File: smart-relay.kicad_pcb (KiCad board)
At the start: 2 copper layers, 16 parts, among them IC1 TMCS1101A4BQDR, J1 Screw_Terminal_01x03, J2 Conn_01x04, K1 G5LE-1, Q1 BSS138K, U1 OPAMP, U2 ATtiny85-20PU

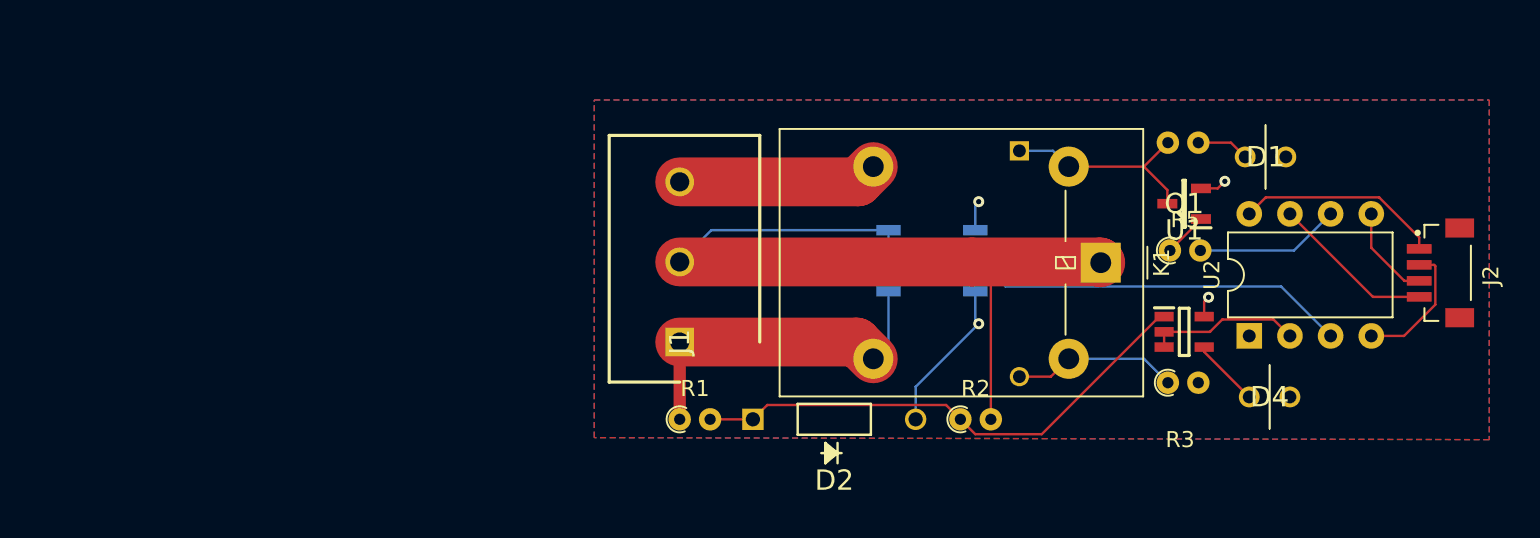
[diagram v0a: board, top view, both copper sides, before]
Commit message: separate hv line
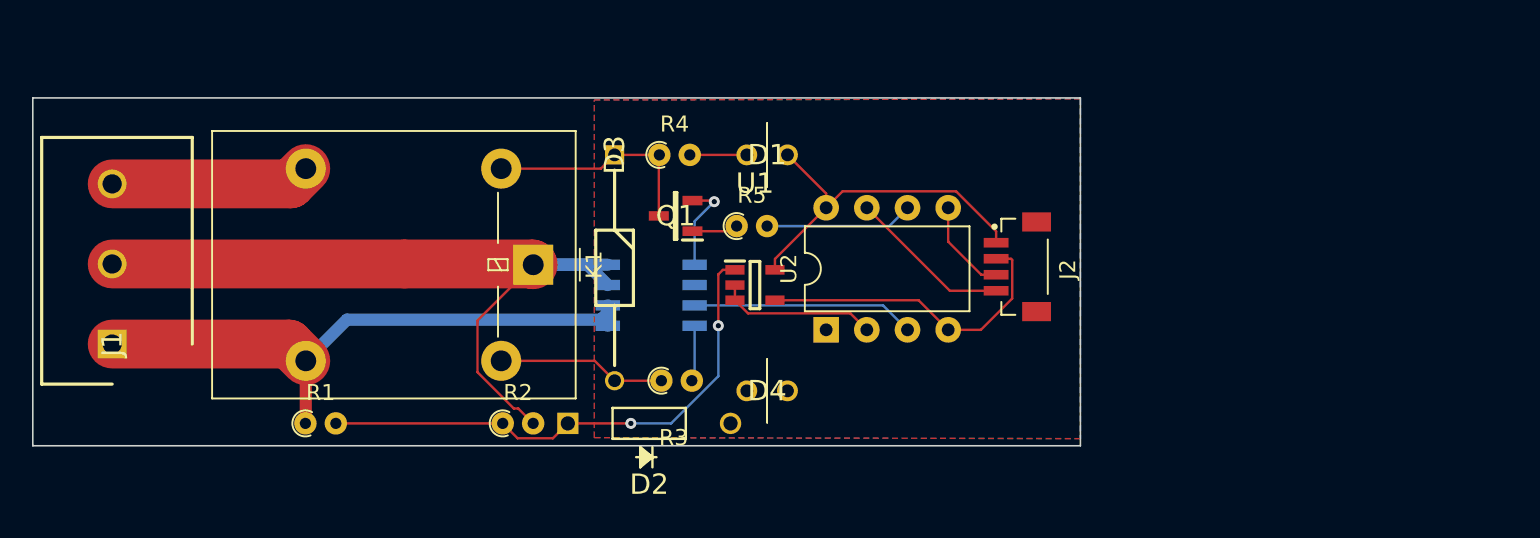
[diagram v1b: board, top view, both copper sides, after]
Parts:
- D3, R4: moved to F.Cu
- moved J1 35.4 mm to (28.4, 63.5)
- moved K1 35.4 mm to (54.7, 58.5)
- moved R4 31.8 mm to (62.6, 51.7)
- moved Q1 31.8 mm to (63.6, 55.5)
- moved R3 31.6 mm to (62.7, 65.8)
- moved D4 31.4 mm to (68.1, 66.4)
- moved D1 31.1 mm to (68.1, 51.7)
- moved R2 28.6 mm to (52.8, 68.5)
- moved R5 27.1 mm to (67.4, 56.1)
- moved U1 27.0 mm to (68.6, 59.8)
- moved J2 26.4 mm to (85.0, 58.7)
- moved U2 26.4 mm to (73.0, 62.6)
- moved D3 25.3 mm to (59.8, 51.7)
- moved R1 23.4 mm to (40.5, 68.5)
- moved IC1 17.7 mm to (62.1, 60.5)
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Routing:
- net NC: track 23.2 -> 37.8 mm
- net ISENSE: track 23.9 -> 13.9 mm
- net GND: track 16.1 -> 25.7 mm, vias 2 -> 1
- net COM: track 51.8 -> 49.1 mm
- net +3V3: track 23.8 -> 25.8 mm, vias 2 -> 0
- net Net-(D2-Pad2): track 32.5 -> 33.4 mm, vias 0 -> 2
- net Net-(D3-Pad1): track 13.2 -> 14.1 mm
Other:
- board outline added: 65.4 x 21.7 mm

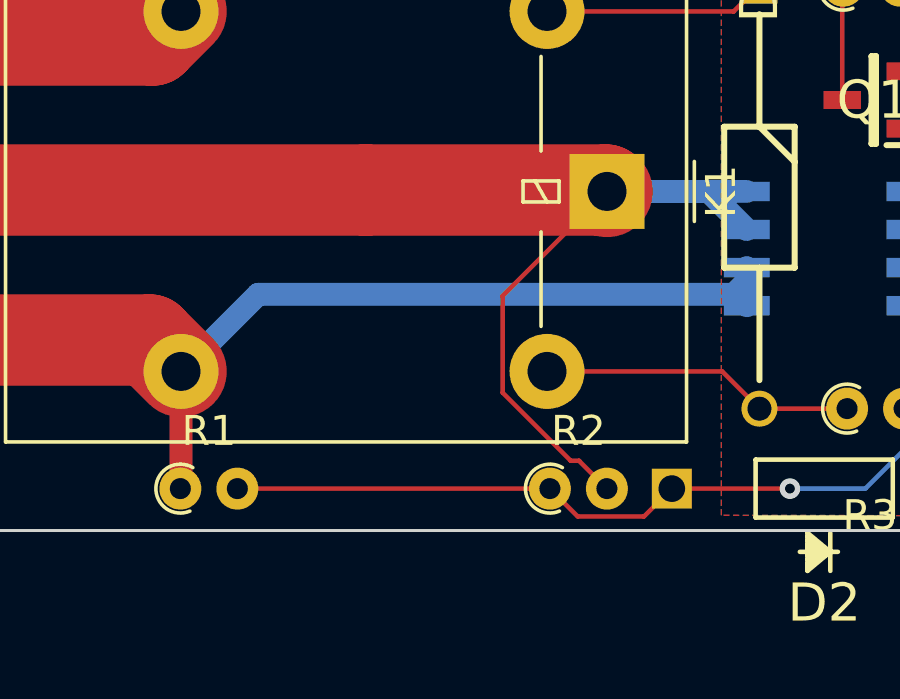
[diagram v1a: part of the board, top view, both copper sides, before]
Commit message: increase trace width for divider
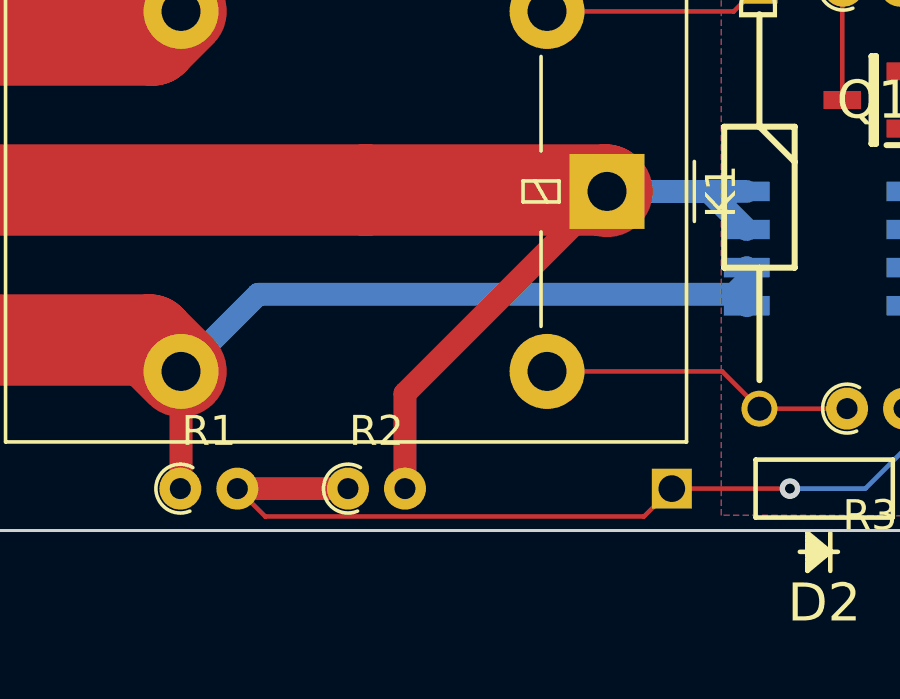
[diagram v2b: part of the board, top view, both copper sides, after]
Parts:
- moved R2 6.73 mm to (46.1, 68.5)
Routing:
- net Net-(D2-Pad2): track 33.4 -> 37.1 mm

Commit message: don't remember
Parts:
- added REF**: MountingHole_2.5mm_Pad, MountingHole:MountingHole_2.5mm_Pad, F.Cu at (26.8, 47.2)
- added REF**: MountingHole_2.5mm_Pad, MountingHole:MountingHole_2.5mm_Pad, F.Cu at (26.8, 69.2)
- added REF**: MountingHole_2.5mm_Pad, MountingHole:MountingHole_2.5mm_Pad, F.Cu at (80.3, 69.2)
- added REF**: MountingHole_2.5mm_Pad, MountingHole:MountingHole_2.5mm_Pad, F.Cu at (80.0, 47.4)
- moved R5 6.13 mm to (62.7, 52.2)
- moved J2 5.21 mm to (79.8, 58.4)
- moved U2 5.09 mm to (67.9, 62.4)
- moved U1 4.83 mm to (63.8, 59.6)
- moved D1 4.45 mm to (68.2, 47.2)
- moved R4 3.45 mm to (59.8, 49.7)
- moved D4 2.81 mm to (68.3, 69.2)
- moved D2 2.41 mm to (54.5, 68.5)
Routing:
- net COM: track 48.8 -> 75.2 mm
- net +3V3: track 25.8 -> 4.43 mm, vias 0 -> 3
- net NC: track 37.8 -> 50.3 mm
- net NO: track 12.5 -> 25.0 mm
- net GND: track 25.7 -> 13.4 mm, vias 1 -> 2
- net Net-(D2-Pad2): track 37.1 -> 26.2 mm, vias 2 -> 0
- net ISENSE: track 13.9 -> 8.74 mm
- net Net-(D1-Pad1): track 3.56 -> 7.48 mm
- net Net-(Q1-Pad1): track 2.89 -> 5.06 mm
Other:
- board size 65.4 x 21.7 mm -> 60.1 x 28.3 mm

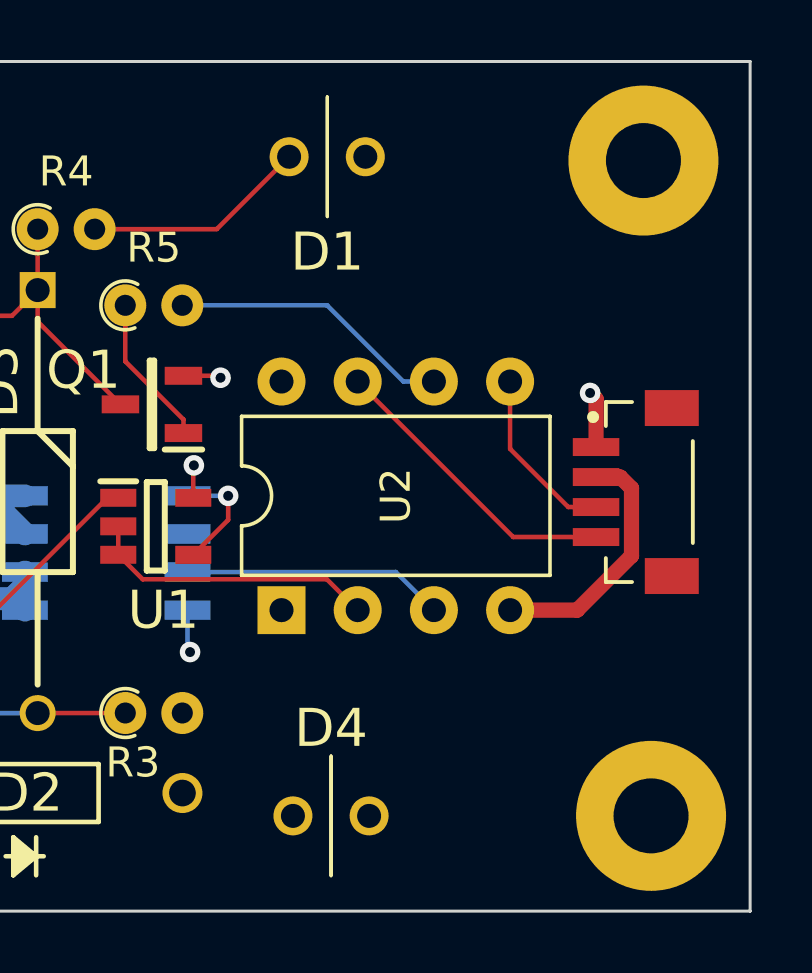
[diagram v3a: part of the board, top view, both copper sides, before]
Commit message: add decoupling cap and headers
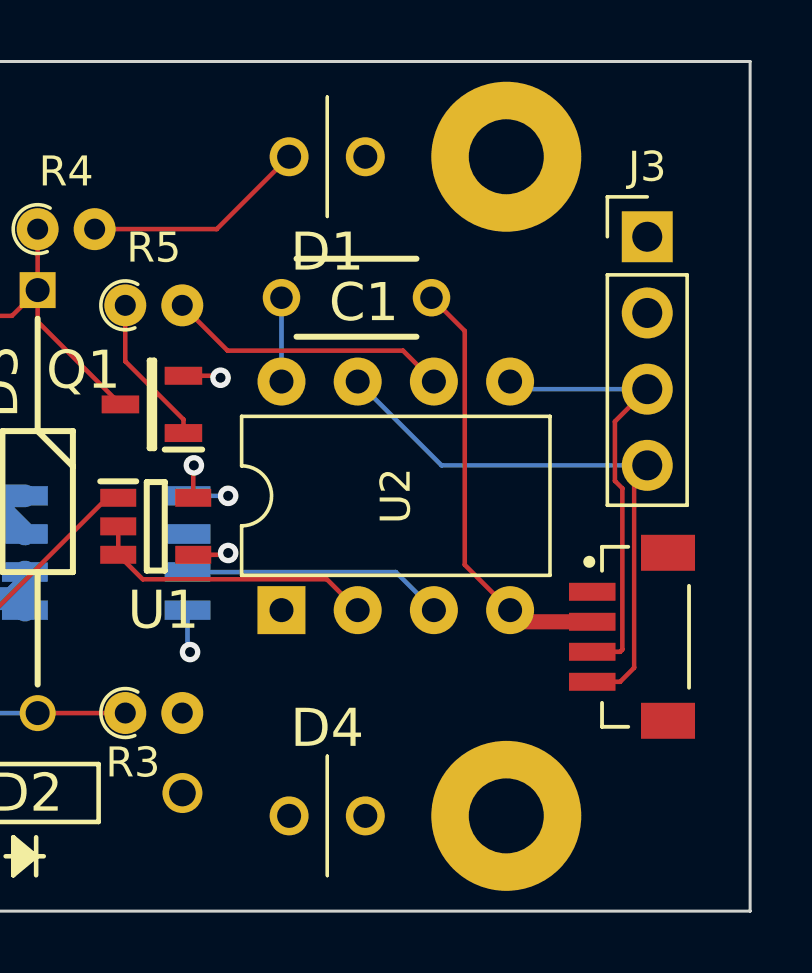
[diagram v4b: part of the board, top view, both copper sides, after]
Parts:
- added C1: C, smart-relay:K104K15X7RF53H5, F.Cu at (70.4, 51.9)
- added J3: Conn_01x04, Connector_PinHeader_2.54mm:PinHeader_1x04_P2.54mm_Vertical, F.Cu at (80.1, 49.9)
- moved J2 4.83 mm to (79.6, 63.2)
- moved REF** 4.83 mm to (75.4, 69.2)
- moved REF** 4.57 mm to (75.4, 47.2)
- moved D4 0.13 mm to (68.2, 69.2)
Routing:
- net SCL: track 10.1 -> 19.3 mm
- net SDA: track 5.91 -> 14.9 mm
- net GND: track 13.4 -> 18.9 mm, vias 2 -> 3
- net +3V3: track 4.43 -> 5.34 mm, vias 3 -> 2

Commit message: add another voltage sensor
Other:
- board text added: "Sense Relay v0 anders@conbere.org"
